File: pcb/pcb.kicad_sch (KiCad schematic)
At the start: 7 parts, among them J11 MountingHole_Pad, J12 MountingHole_Pad, J13 MountingHole_Pad, J14 MountingHole_Pad

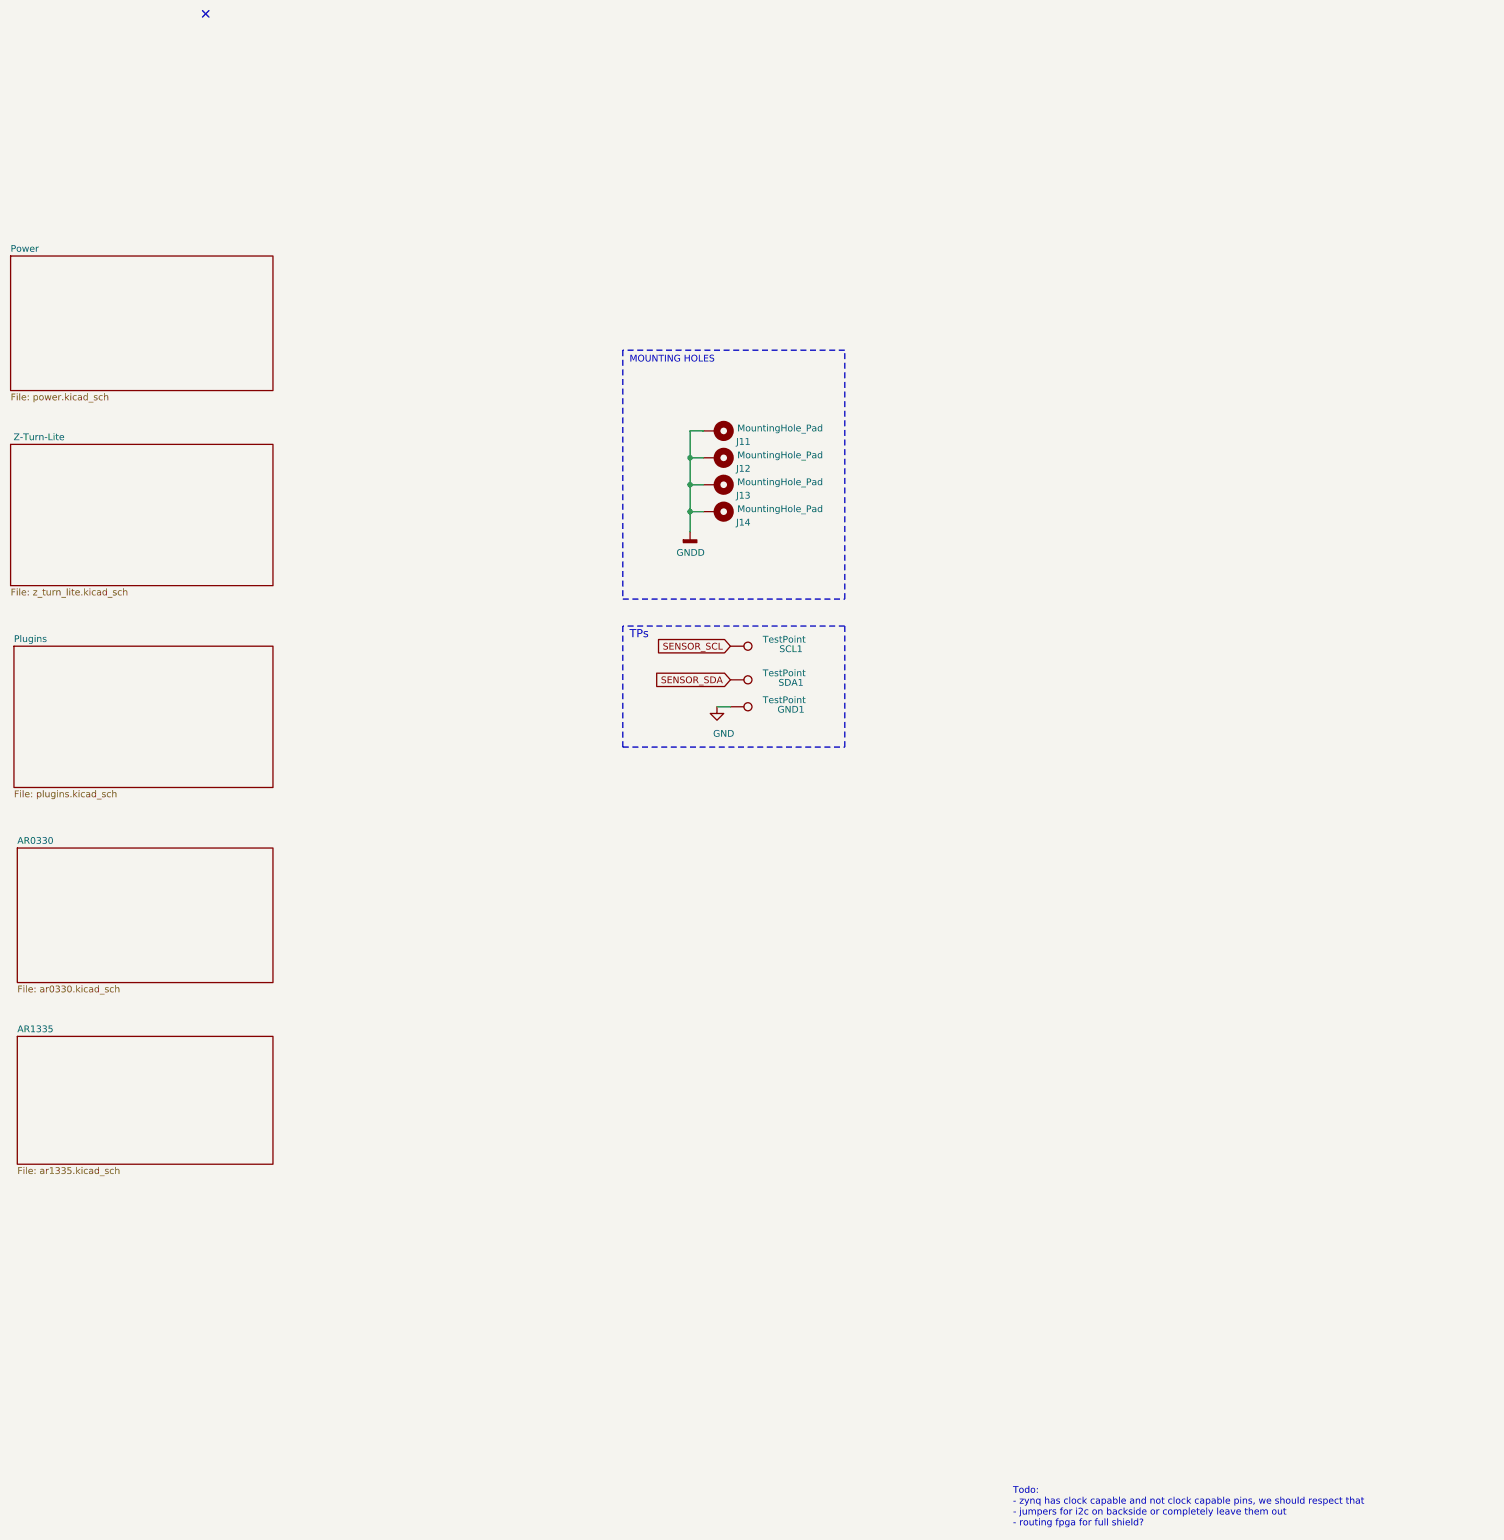
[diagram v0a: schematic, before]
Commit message: refinements; add ar1335 footprint
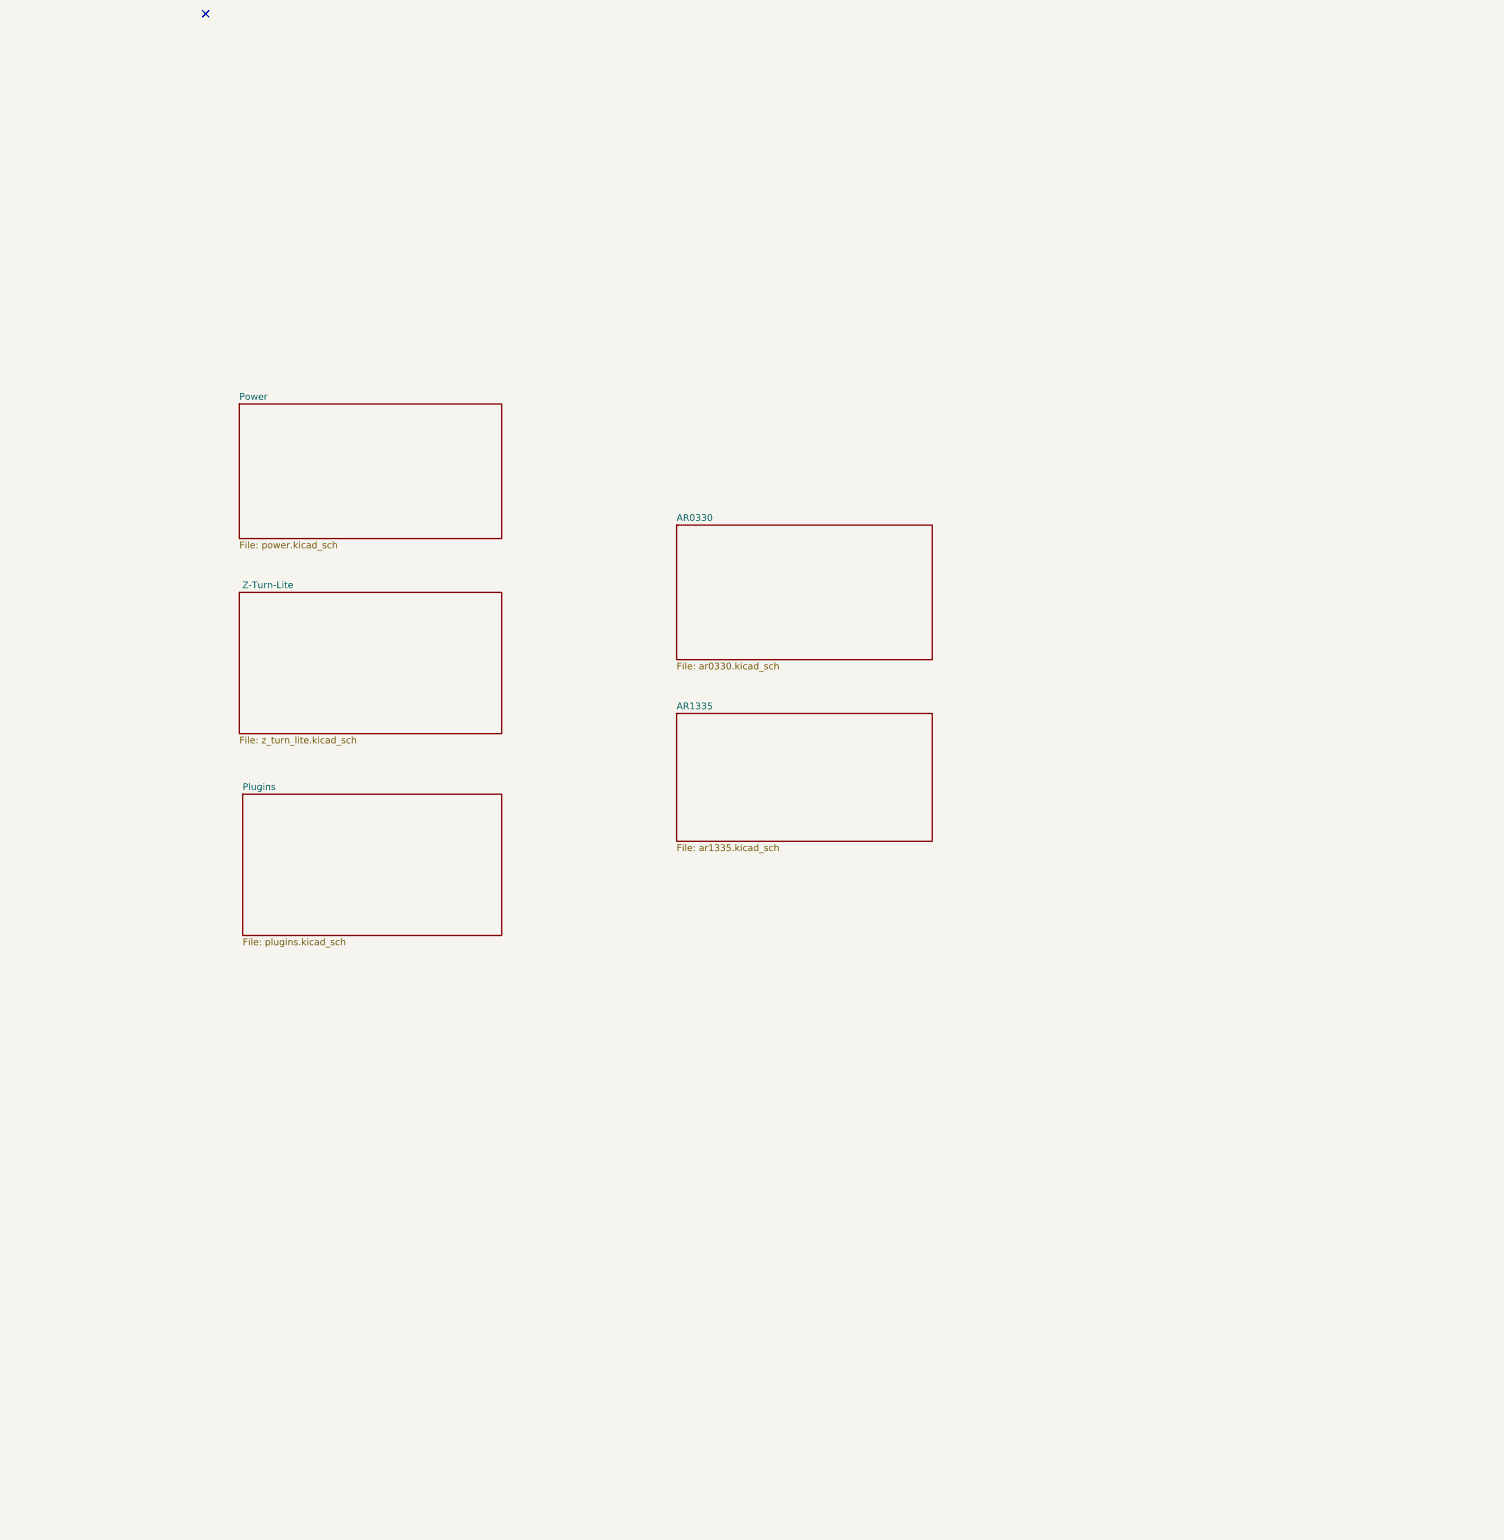
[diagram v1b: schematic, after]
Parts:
- removed GND1, SCL1, SDA1: TestPoint, Connectors_TestPoints:Test_Point_Pad_2.0x2.0mm, symbol Connector:TestPoint
- removed J11, J12, J13, J14: MountingHole_Pad, Mounting_Holes:MountingHole_3.2mm_M3_Pad, symbol Mechanical:MountingHole_Pad
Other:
- note removed: "MOUNTING HOLES"
- note removed: "TPs"
- note removed: "Todo: - zynq has clock capable and not clock capable pins, we should respect that - jumpers for i2c on backside or completely leave them out - routing fpga for full shield?"

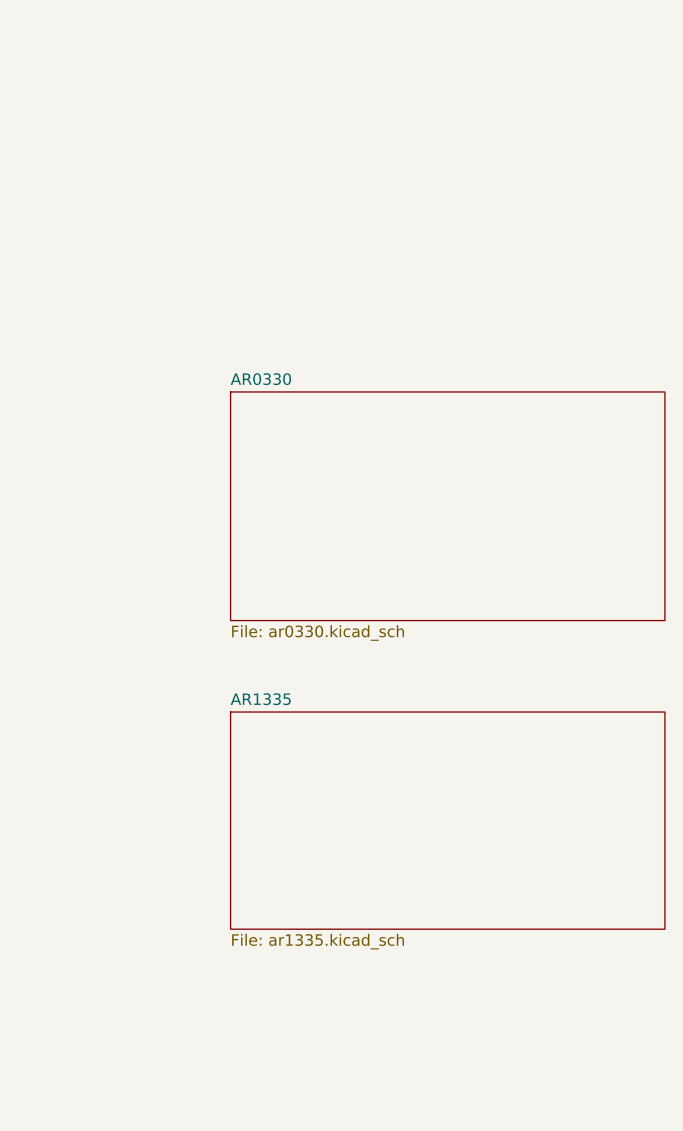
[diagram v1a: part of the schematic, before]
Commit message: Change Plans: two image sensors
* Redo power management
* Add level shifters
* Intention to use both image sensors on the same board
* Add Pmod & LEDs
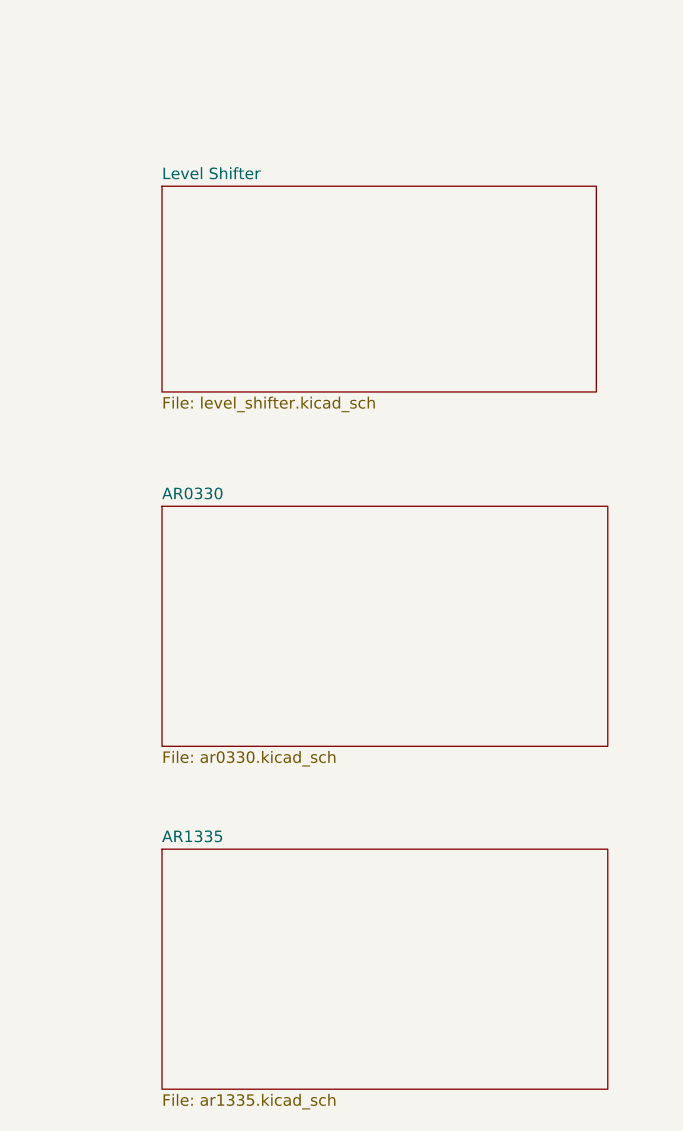
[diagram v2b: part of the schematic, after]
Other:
- added sheet Level Shifter (level_shifter.kicad_sch)

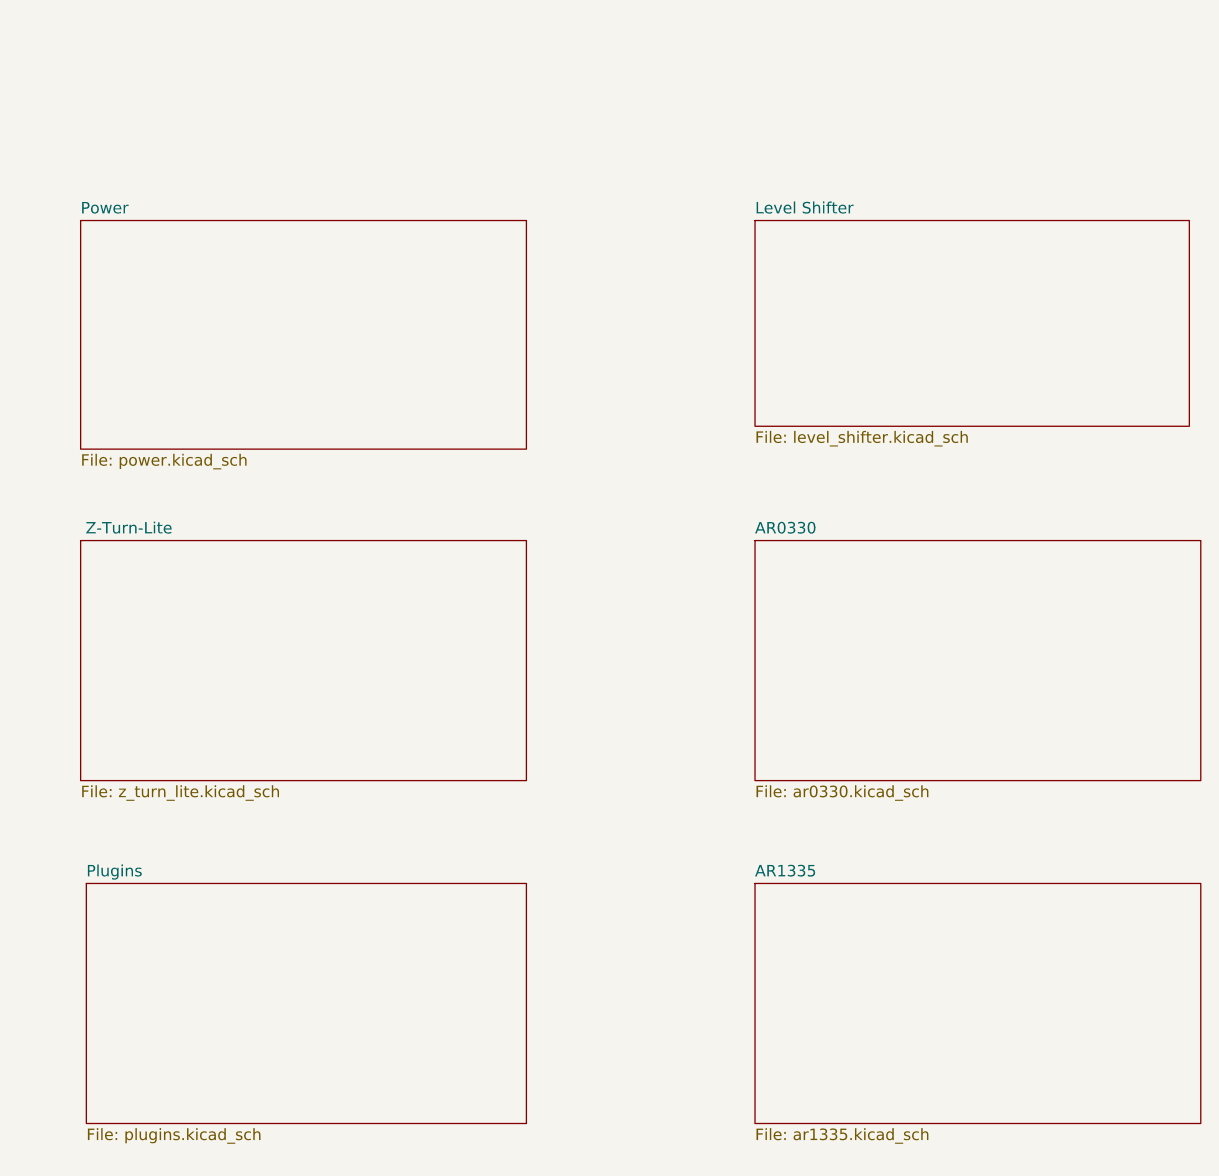
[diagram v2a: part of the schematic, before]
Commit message: add i2c addresses
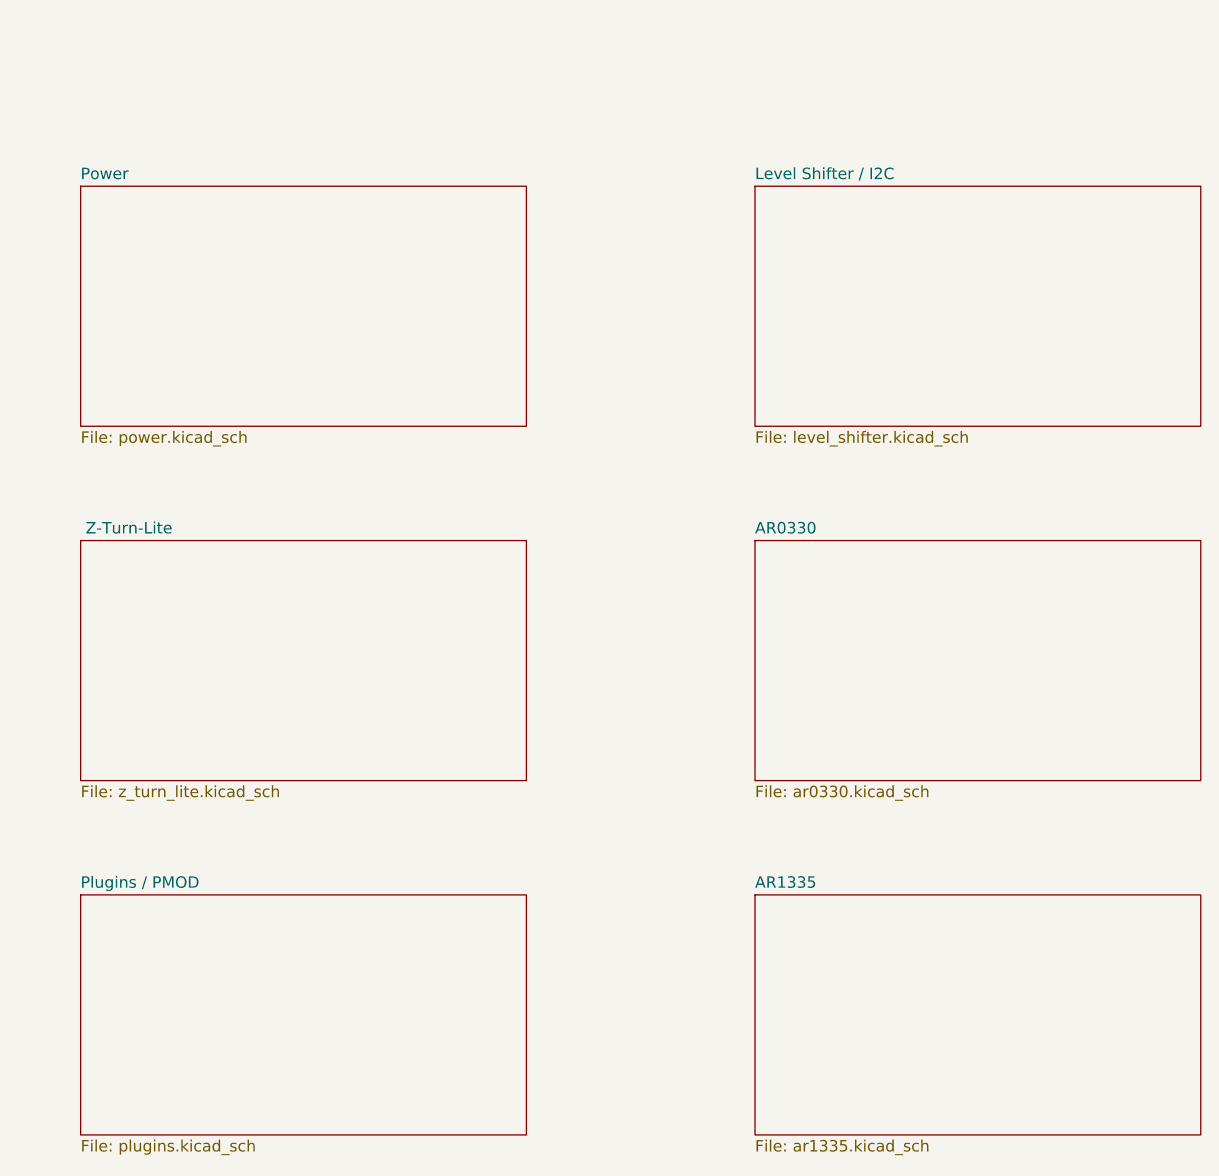
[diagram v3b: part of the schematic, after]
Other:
- sheet Level Shifter renamed Level Shifter / I2C
- sheet Plugins renamed Plugins / PMOD
